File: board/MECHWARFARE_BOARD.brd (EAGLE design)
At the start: 44.5 x 83.8 mm, 8 parts, among them J1 5267-3, Q2 FDD4141TO252

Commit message: giving access to necessary libs
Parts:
- removed J1: 5267-3, con-molex-spox:5267-3
- removed TURRET_PWR, TURRET_PWR1: XT60, XT60:XT60
- added J2: 5267-3, con-molex-spox:5267-3
- added U$1, U$2: XT60, XT60:XT60
- renumbered MS1 to MS2
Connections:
- net GND: now also J2.P$3, U$1.-, U$2.-; no longer J1.P$3, TURRET_PWR.-, TURRET_PWR1.-
- net MOTOR_CMD: now also J2.P$1; no longer J1.P$1
- net MOTOR_POWER: now also J2.P$2, U$1.+; no longer J1.P$2, TURRET_PWR1.+
- net TURRET_POS: now also U$2.+; no longer TURRET_PWR.+
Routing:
- net MOTOR_CMD: track 26.7 -> 20.9 mm
- net TURRET_POS: track 22.6 -> 25.6 mm
- net MOTOR_POWER: track 16.8 -> 16.0 mm
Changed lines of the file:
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@@
 <attribute name="VALUE" x="28.575" y="11.43" size="1.27" layer="27" rot="R90"/>
 </element>
-<element name="MS1" library="ME507" package="FEATHERWING" value="FEATHERWINGEXTENDED_BOTH_ENDS" x="11.43" y="78.74" smashed="yes" rot="R270"/>
 <element name="Q2" library="transistor-fet" library_urn="urn:adsk.eagle:library:396" package="TO252" package3d_urn="urn:adsk.eagle:package:28537/2" value="FDD4141TO252" x="21.59" y="24.13" smashed="yes" rot="R270">
 <attribute name="NAME" x="19.05" y="27.94" size="1.27" layer="25"/>
@@
 <attribute name="VALUE" x="19.685" y="40.64" size="1.27" layer="27" rot="R180"/>
 </element>
-<element name="TURRET_PWR" library="XT60" package="XT60" value="XT60" x="44.45" y="5.08" smashed="yes" rot="R180"/>
-<element name="TURRET_PWR1" library="XT60" package="XT60" value="XT60" x="16.51" y="5.08" smashed="yes" rot="R180"/>
 <element name="X3" library="ME507" package="2POL254" value="" x="39.37" y="13.97" smashed="yes" rot="R90">
 <attribute name="NAME" x="35.052" y="11.176" size="1.27" layer="25" rot="R90"/>
 <attribute name="VALUE" x="44.958" y="11.176" size="1.27" layer="27" rot="R90"/>
 </element>
-<element name="J1" library="con-molex-spox" package="5267-3" value="5267-3" x="5.08" y="17.78" smashed="yes" rot="R270">
-<attribute name="NAME" x="6.35" y="19.05" size="1.27" layer="21" rot="R270"/>
-<attribute name="VALUE" x="0" y="20.32" size="1.27" layer="21" rot="R270"/>
+<element name="U$1" library="XT60" package="XT60" value="XT60" x="1.27" y="5.08" smashed="yes"/>
+<element name="U$2" library="XT60" package="XT60" value="XT60" x="27.94" y="5.08" smashed="yes"/>
+<element name="J2" library="con-molex-spox" package="5267-3" value="5267-3" x="5.08" y="19.05" smashed="yes" rot="R270">
+<attribute name="NAME" x="7.62" y="21.59" size="1.27" layer="21" rot="R270"/>
+<attribute name="VALUE" x="0" y="21.59" size="1.27" layer="21" rot="R270"/>
 </element>
+<element name="MS2" library="ME507" package="FEATHERWING" value="FEATHERWINGEXTENDED_BOTH_ENDS" x="11.43" y="78.74" smashed="yes" rot="R270"/>
 </elements>
 <signals>
@@
 <signal name="TURRET_POS">
 <contactref element="D1" pad="C"/>
-<contactref element="TURRET_PWR" pad="+"/>
 <contactref element="X3" pad="1"/>
 <wire x1="39.37" y1="12.7" x2="39.95" y2="12.12" width="0.6096" layer="1"/>
-<wire x1="39.95" y1="12.12" x2="39.95" y2="5.08" width="0.6096" layer="1"/>
 <wire x1="39.37" y1="12.7" x2="38.1" y2="11.43" width="0.6096" layer="1"/>
 <wire x1="25.915" y1="11.43" x2="25.4" y2="11.945" width="0.6096" layer="1"/>
 <wire x1="38.1" y1="11.43" x2="25.915" y2="11.43" width="0.6096" layer="1"/>
+<contactref element="U$2" pad="+"/>
+<wire x1="32.44" y1="5.08" x2="32.265" y2="5.08" width="0.508" layer="1"/>
+<wire x1="32.44" y1="5.08" x2="25.575" y2="11.945" width="0.6096" layer="1"/>
+<wire x1="25.575" y1="11.945" x2="25.4" y2="11.945" width="0.6096" layer="1"/>
 </signal>
 <signal name="GND">
 <contactref element="Q2" pad="3"/>
-<contactref element="TURRET_PWR" pad="-"/>
-<contactref element="MS1" pad="4"/>
-<contactref element="TURRET_PWR1" pad="-"/>
 <polygon width="0.1524" layer="1">
 <vertex x="0" y="83.82"/>
@@
 <vertex x="44.45" y="83.82"/>
 </polygon>
-<contactref element="J1" pad="P$3"/>
+<contactref element="U$1" pad="-"/>
+<contactref element="U$2" pad="-"/>
+<contactref element="J2" pad="P$3"/>
+<contactref element="MS2" pad="4"/>
 </signal>
 <signal name="N$21">
 <contactref element="R1" pad="1"/>
-<contactref element="MS1" pad="19"/>
 <wire x1="20" y1="38.1" x2="21.27" y2="39.37" width="0.6096" layer="1"/>
+<contactref element="MS2" pad="19"/>
 <wire x1="21.27" y1="39.37" x2="33.02" y2="39.37" width="0.6096" layer="1"/>
 </signal>
 <signal name="MOTOR_POWER">
-<contactref element="TURRET_PWR1" pad="+"/>
-<contactref element="J1" pad="P$2"/>
-<wire x1="5.08" y1="15.28" x2="11.4032625" y2="15.2132625" width="0.6096" layer="1"/>
-<wire x1="11.39" y1="15.2" x2="11.4032625" y2="15.2132625" width="0.6096" layer="1"/>
-<wire x1="11.4032625" y1="15.2132625" x2="11.43" y2="15.24" width="0.6096" layer="1"/>
-<wire x1="12.01" y1="5.08" x2="12.01" y2="14.58" width="0.6096" layer="1"/>
-<wire x1="12.01" y1="14.58" x2="11.39" y2="15.2" width="0.6096" layer="1"/>
+<contactref element="U$1" pad="+"/>
+<contactref element="J2" pad="P$2"/>
+<wire x1="5.08" y1="16.55" x2="6.35" y2="16.55" width="0.508" layer="1"/>
+<wire x1="5.08" y1="16.55" x2="7.58" y2="16.55" width="0.6096" layer="1"/>
+<wire x1="7.58" y1="16.55" x2="7.62" y2="16.51" width="0.6096" layer="1"/>
+<wire x1="7.62" y1="6.93" x2="5.77" y2="5.08" width="0.6096" layer="1"/>
+<wire x1="7.62" y1="16.51" x2="7.62" y2="6.93" width="0.6096" layer="1"/>
 </signal>
 <signal name="MOTOR_CMD">
-<contactref element="J1" pad="P$1"/>
-<contactref element="MS1" pad="15"/>
-<wire x1="5.08" y1="17.78" x2="5.08" y2="36.83" width="0.6096" layer="1"/>
-<wire x1="5.08" y1="36.83" x2="12.7" y2="36.83" width="0.6096" layer="1"/>
+<contactref element="J2" pad="P$1"/>
+<wire x1="5.08" y1="19.05" x2="5.08" y2="29.21" width="0.6096" layer="1"/>
+<contactref element="MS2" pad="15"/>
+<wire x1="5.08" y1="29.21" x2="12.7" y2="36.83" width="0.6096" layer="1"/>
 </signal>
 </signals>

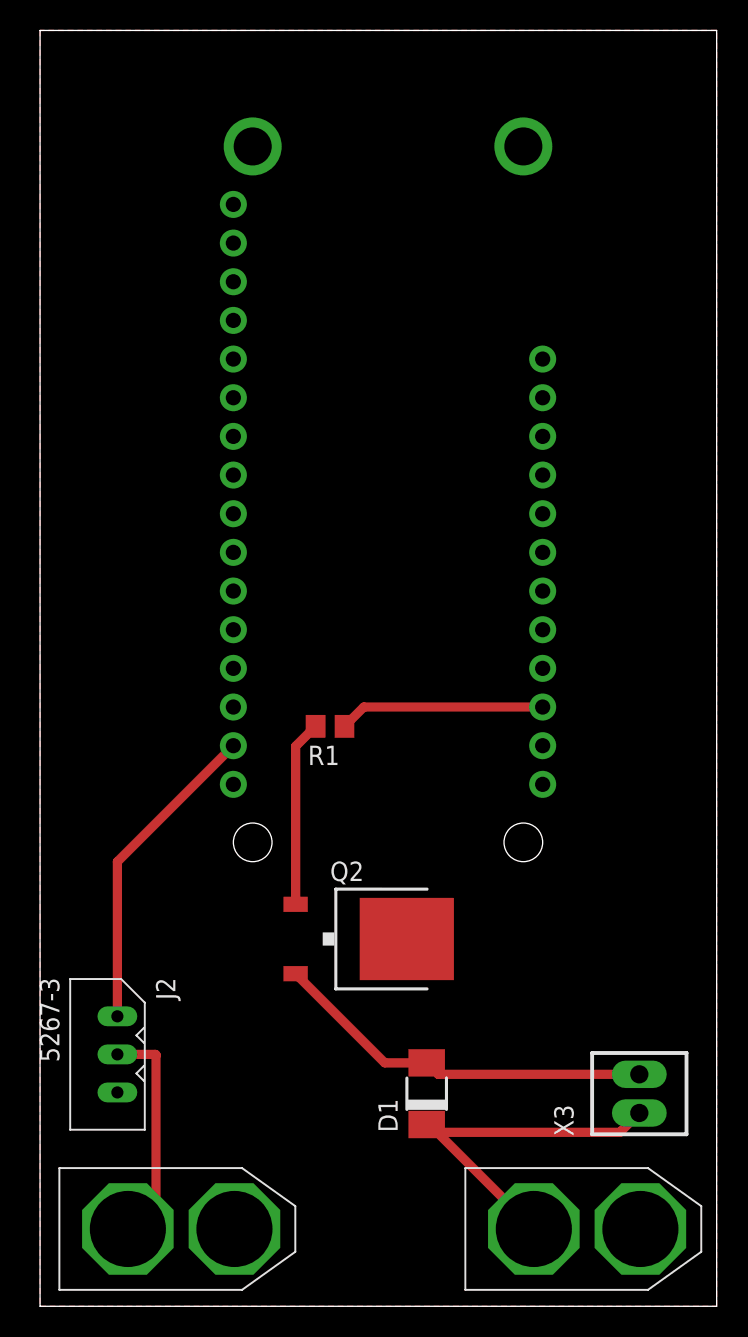
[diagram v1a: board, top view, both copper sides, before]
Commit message: Connector Change
Switched back to xt60 and removed duplicate files.
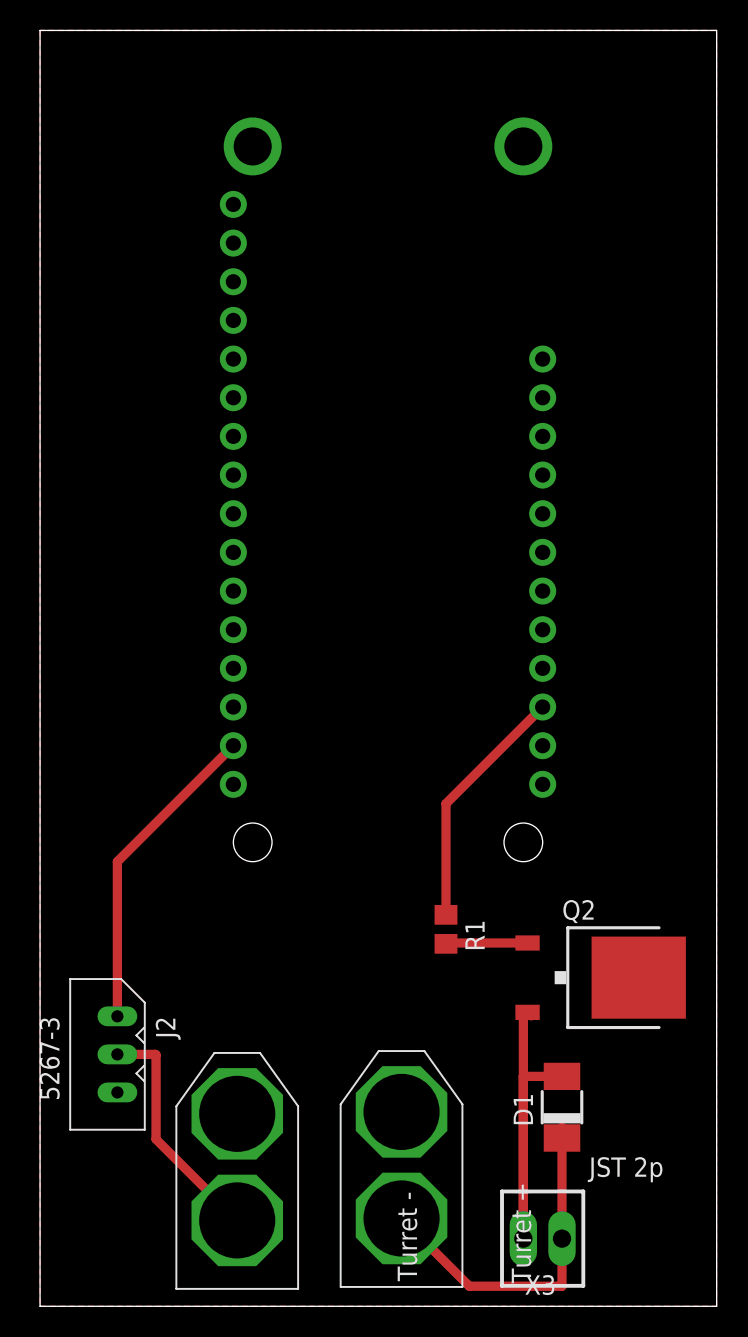
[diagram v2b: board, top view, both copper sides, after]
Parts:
- moved Q2 15.5 mm to (36.8, 21.6)
- moved R1 15.4 mm to (26.7, 24.8), turned to 270 degrees
- moved U$1 12.3 mm to (13.0, 1.14), turned to 90 degrees
- moved X3 11.4 mm to (33.0, 4.45), turned to 180 degrees
- moved D1 8.93 mm to (34.3, 13.1)
- moved U$2 5.66 mm to (23.7, 1.27), turned to 90 degrees
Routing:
- net GATE: track 12.2 -> 5.38 mm
- net TURRET_NEG: track 25.7 -> 28.5 mm
- net TURRET_POS: track 25.6 -> 22.8 mm
- net N$21: track 13.5 -> 16.3 mm
- net MOTOR_POWER: track 16.0 -> 16.9 mm
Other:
- board text added: "JST 2p"
- board text added: "KL AT CS"
- board text added: "Mech Warfare 2022"
- board text added: "Turret +"
- board text added: "Turret -"
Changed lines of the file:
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@@
 <board>
 <plain>
+<text x="32.258" y="1.524" size="1.27" layer="25" rot="R90">Turret +</text>
+<text x="24.765" y="1.651" size="1.27" layer="25" rot="R90">Turret -</text>
+<text x="36.068" y="8.509" size="1.27" layer="25">JST 2p</text>
+<circle x="22.987" y="23.749" radius="21.849903125" width="0.6096" layer="26"/>
+<wire x1="39.37" y1="22.86" x2="6.35" y2="22.86" width="0.6096" layer="26" curve="-175.594804"/>
+<circle x="13.97" y="30.48" radius="2.83980625" width="0.6096" layer="26"/>
+<circle x="31.75" y="30.48" radius="2.83980625" width="0.6096" layer="26"/>
+<text x="36.83" y="44.45" size="1.778" layer="26" rot="MR90">KL AT CS</text>
+<text x="40.64" y="40.64" size="1.778" layer="26" rot="MR90">Mech Warfare 2022</text>
 </plain>
 <attributes>
@@
 </autorouter>
 <elements>
-<element name="D1" library="diode" library_urn="urn:adsk.eagle:library:210" package="DO-214AC" package3d_urn="urn:adsk.eagle:package:43416/2" value="" x="25.4" y="13.97" smashed="yes" rot="R90">
-<attribute name="NAME" x="23.495" y="11.43" size="1.27" layer="25" rot="R90"/>
-<attribute name="POPULARITY" value="25" x="68.58" y="53.34" size="1.778" layer="27" rot="R90" display="off"/>
-<attribute name="VALUE" x="28.575" y="11.43" size="1.27" layer="27" rot="R90"/>
-</element>
-<element name="Q2" library="transistor-fet" library_urn="urn:adsk.eagle:library:396" package="TO252" package3d_urn="urn:adsk.eagle:package:28537/2" value="FDD4141TO252" x="21.59" y="24.13" smashed="yes" rot="R270">
-<attribute name="NAME" x="19.05" y="27.94" size="1.27" layer="25"/>
-<attribute name="POPULARITY" value="3" x="-8.89" y="5.08" size="1.778" layer="27" rot="R270" display="off"/>
-<attribute name="VALUE" x="19.05" y="19.05" size="1.27" layer="27"/>
-</element>
-<element name="R1" library="rcl" library_urn="urn:adsk.eagle:library:334" package="R0805" package3d_urn="urn:adsk.eagle:package:23553/2" value="100" x="19.05" y="38.1" smashed="yes" rot="R180">
-<attribute name="NAME" x="19.685" y="36.83" size="1.27" layer="25" rot="R180"/>
-<attribute name="POPULARITY" value="85" x="-15.24" y="83.82" size="1.778" layer="27" rot="R180" display="off"/>
-<attribute name="SPICEPREFIX" value="R" x="-15.24" y="83.82" size="1.778" layer="27" rot="R180" display="off"/>
-<attribute name="VALUE" x="19.685" y="40.64" size="1.27" layer="27" rot="R180"/>
-</element>
-<element name="X3" library="ME507" package="2POL254" value="" x="39.37" y="13.97" smashed="yes" rot="R90">
-<attribute name="NAME" x="35.052" y="11.176" size="1.27" layer="25" rot="R90"/>
-<attribute name="VALUE" x="44.958" y="11.176" size="1.27" layer="27" rot="R90"/>
-</element>
-<element name="U$1" library="XT60" package="XT60" value="XT60" x="1.27" y="5.08" smashed="yes"/>
-<element name="U$2" library="XT60" package="XT60" value="XT60" x="27.94" y="5.08" smashed="yes"/>
+<element name="D1" library="diode" library_urn="urn:adsk.eagle:library:210" package="DO-214AC" package3d_urn="urn:adsk.eagle:package:43416/2" value="" x="34.29" y="13.081" smashed="yes" rot="R90">
+<attribute name="NAME" x="32.385" y="11.811" size="1.27" layer="25" rot="R90"/>
+<attribute name="POPULARITY" value="25" x="77.47" y="52.451" size="1.778" layer="27" rot="R90" display="off"/>
+<attribute name="VALUE" x="37.465" y="10.541" size="1.27" layer="27" rot="R90"/>
+</element>
+<element name="Q2" library="transistor-fet" library_urn="urn:adsk.eagle:library:396" package="TO252" package3d_urn="urn:adsk.eagle:package:28537/2" value="FDD4141TO252" x="36.83" y="21.59" smashed="yes" rot="R270">
+<attribute name="NAME" x="34.29" y="25.4" size="1.27" layer="25"/>
+<attribute name="POPULARITY" value="3" x="6.35" y="2.54" size="1.778" layer="27" rot="R270" display="off"/>
+</element>
+<element name="R1" library="rcl" library_urn="urn:adsk.eagle:library:334" package="R0805" package3d_urn="urn:adsk.eagle:package:23553/2" value="100" x="26.67" y="24.765" smashed="yes" rot="R270">
+<attribute name="NAME" x="27.94" y="25.4" size="1.27" layer="25" rot="R270"/>
+<attribute name="POPULARITY" value="85" x="-19.05" y="-9.525" size="1.778" layer="27" rot="R270" display="off"/>
+<attribute name="SPICEPREFIX" value="R" x="-19.05" y="-9.525" size="1.778" layer="27" rot="R270" display="off"/>
+<attribute name="VALUE" x="24.13" y="25.4" size="1.27" layer="27" rot="R270"/>
+</element>
+<element name="X3" library="ME507" package="2POL254" value="" x="33.02" y="4.445" smashed="yes" rot="R180">
+<attribute name="NAME" x="33.909" y="2.032" size="1.27" layer="25" rot="R180"/>
+<attribute name="VALUE" x="35.814" y="10.033" size="1.27" layer="27" rot="R180"/>
+</element>
+<element name="U$1" library="XT60" package="XT60" value="XT60" x="12.954" y="1.143" smashed="yes" rot="R90"/>
 <element name="J2" library="con-molex-spox" package="5267-3" value="5267-3" x="5.08" y="19.05" smashed="yes" rot="R270">
-<attribute name="NAME" x="7.62" y="21.59" size="1.27" layer="21" rot="R270"/>
-<attribute name="VALUE" x="0" y="21.59" size="1.27" layer="21" rot="R270"/>
+<attribute name="NAME" x="7.62" y="19.05" size="1.27" layer="21" rot="R270"/>
+<attribute name="VALUE" x="0" y="19.05" size="1.27" layer="21" rot="R270"/>
 </element>
 <element name="MS2" library="ME507" package="FEATHERWING" value="FEATHERWINGEXTENDED_BOTH_ENDS" x="11.43" y="78.74" smashed="yes" rot="R270"/>
+<element name="U$2" library="XT60" package="XT60" value="XT60" x="23.749" y="1.27" smashed="yes" rot="R90"/>
 </elements>
 <signals>
@@
 <contactref element="R1" pad="2"/>
 <contactref element="Q2" pad="1"/>
-<wire x1="16.79" y1="26.41" x2="16.79" y2="36.79" width="0.6096" layer="1"/>
-<wire x1="16.79" y1="36.79" x2="18.1" y2="38.1" width="0.6096" layer="1"/>
+<wire x1="26.67" y1="23.815" x2="26.725" y2="23.87" width="0.6096" layer="1"/>
+<wire x1="26.725" y1="23.87" x2="32.03" y2="23.87" width="0.6096" layer="1"/>
 </signal>
 <signal name="TURRET_NEG">
@@
 <contactref element="Q2" pad="2"/>
 <contactref element="X3" pad="2"/>
-<wire x1="16.79" y1="21.85" x2="17.025" y2="21.615" width="0.6096" layer="1"/>
-<wire x1="39.37" y1="15.24" x2="26.155" y2="15.24" width="0.6096" layer="1"/>
-<wire x1="26.155" y1="15.24" x2="25.4" y2="15.995" width="0.6096" layer="1"/>
-<wire x1="16.79" y1="21.85" x2="22.645" y2="15.995" width="0.6096" layer="1"/>
-<wire x1="22.645" y1="15.995" x2="25.4" y2="15.995" width="0.6096" layer="1"/>
+<wire x1="32.03" y1="19.31" x2="32.265" y2="19.075" width="0.6096" layer="1"/>
+<wire x1="32.03" y1="19.31" x2="31.75" y2="19.03" width="0.6096" layer="1"/>
+<wire x1="31.75" y1="4.445" x2="31.75" y2="19.03" width="0.6096" layer="1"/>
+<wire x1="31.75" y1="15.106" x2="34.29" y2="15.106" width="0.6096" layer="1"/>
+<wire x1="31.75" y1="4.445" x2="31.75" y2="15.106" width="0.6096" layer="1"/>
 </signal>
 <signal name="TURRET_POS">
 <contactref element="D1" pad="C"/>
 <contactref element="X3" pad="1"/>
-<wire x1="39.37" y1="12.7" x2="39.95" y2="12.12" width="0.6096" layer="1"/>
-<wire x1="39.37" y1="12.7" x2="38.1" y2="11.43" width="0.6096" layer="1"/>
-<wire x1="25.915" y1="11.43" x2="25.4" y2="11.945" width="0.6096" layer="1"/>
-<wire x1="38.1" y1="11.43" x2="25.915" y2="11.43" width="0.6096" layer="1"/>
+<wire x1="34.29" y1="11.77" x2="34.29" y2="11.056" width="0.6096" layer="1"/>
+<wire x1="34.29" y1="4.445" x2="34.29" y2="11.056" width="0.6096" layer="1"/>
 <contactref element="U$2" pad="+"/>
-<wire x1="32.44" y1="5.08" x2="32.265" y2="5.08" width="0.508" layer="1"/>
-<wire x1="32.44" y1="5.08" x2="25.575" y2="11.945" width="0.6096" layer="1"/>
-<wire x1="25.575" y1="11.945" x2="25.4" y2="11.945" width="0.6096" layer="1"/>
+<wire x1="23.749" y1="5.77" x2="28.1982" y2="1.3208" width="0.6096" layer="1"/>
+<wire x1="28.1982" y1="1.3208" x2="34.29" y2="1.3208" width="0.6096" layer="1"/>
+<wire x1="34.29" y1="1.3208" x2="34.29" y2="4.445" width="0.6096" layer="1"/>
 </signal>
 <signal name="GND">
@@
 </polygon>
 <contactref element="U$1" pad="-"/>
-<contactref element="U$2" pad="-"/>
 <contactref element="J2" pad="P$3"/>
 <contactref element="MS2" pad="4"/>
+<contactref element="U$2" pad="-"/>
 </signal>
 <signal name="N$21">
 <contactref element="R1" pad="1"/>
-<wire x1="20" y1="38.1" x2="21.27" y2="39.37" width="0.6096" layer="1"/>
 <contactref element="MS2" pad="19"/>
-<wire x1="21.27" y1="39.37" x2="33.02" y2="39.37" width="0.6096" layer="1"/>
+<wire x1="26.67" y1="25.715" x2="26.67" y2="33.02" width="0.6096" layer="1"/>
+<wire x1="26.67" y1="33.02" x2="33.02" y2="39.37" width="0.6096" layer="1"/>
 </signal>
 <signal name="MOTOR_POWER">
@@
 <wire x1="5.08" y1="16.55" x2="7.58" y2="16.55" width="0.6096" layer="1"/>
 <wire x1="7.58" y1="16.55" x2="7.62" y2="16.51" width="0.6096" layer="1"/>
-<wire x1="7.62" y1="6.93" x2="5.77" y2="5.08" width="0.6096" layer="1"/>
-<wire x1="7.62" y1="16.51" x2="7.62" y2="6.93" width="0.6096" layer="1"/>
+<wire x1="12.954" y1="5.643" x2="7.62" y2="10.977" width="0.6096" layer="1"/>
+<wire x1="7.62" y1="16.51" x2="7.62" y2="10.977" width="0.6096" layer="1"/>
 </signal>
 <signal name="MOTOR_CMD">
